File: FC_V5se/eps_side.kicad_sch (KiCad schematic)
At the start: 65 parts, among them IC6 LT3652IMSE#PBF, J10 INHIBIT_P2, J11 DF11CZ-12DP-2V(27), J14 Battery Input, J17 Face4 (Z- Face), J19 ISS_INHIBIT, J2 DF11CZ-12DP-2V(27), J20 RBF_Inhibit, J21 Heater Output, J23 Aux Deploy 1, J24 Deploy 2, J29 INHIBIT_S2, J7 INHIBIT_P1, J8 INHIBIT_S1, U10 TPS54226PWPRPWP14_2P31X2P46-L, U12 LT8610ABEMSE#TRPBF, U16 INA219AxDCN, U8 INA219AxDCN, U9 MCP23017_SS

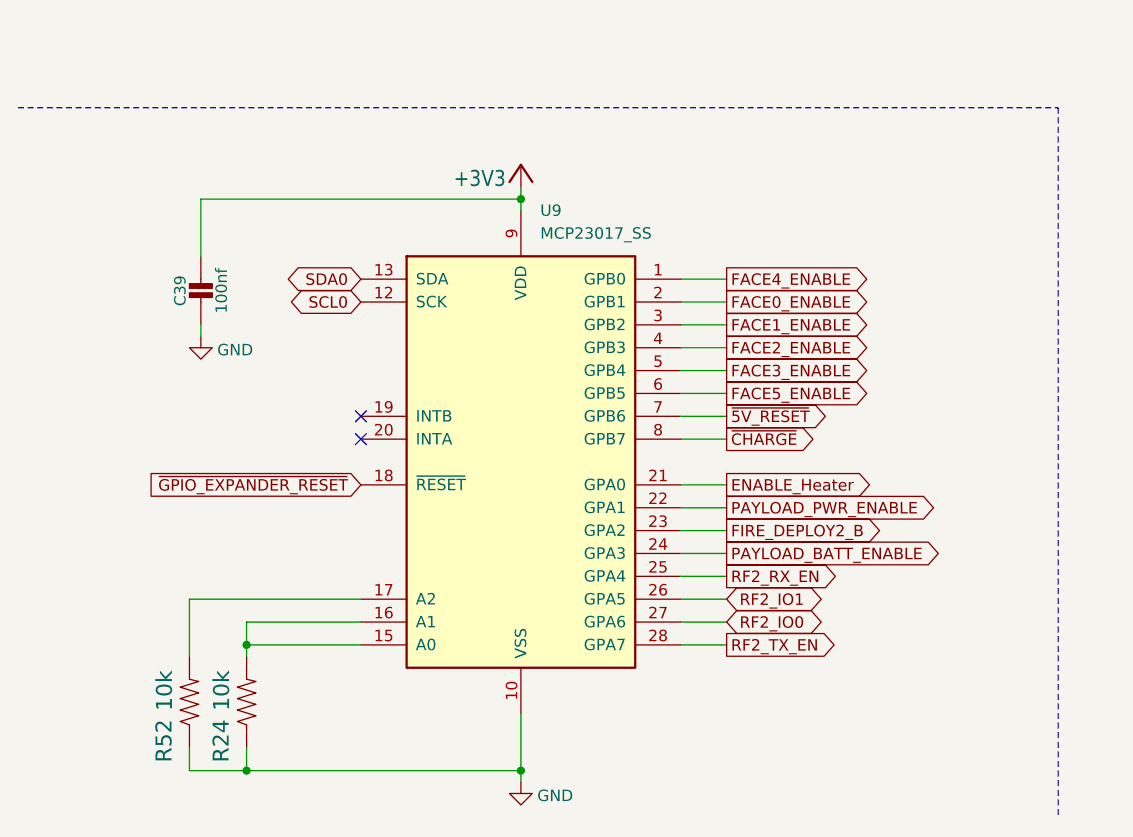
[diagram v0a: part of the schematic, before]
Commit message: V5e: Delete MCP23017
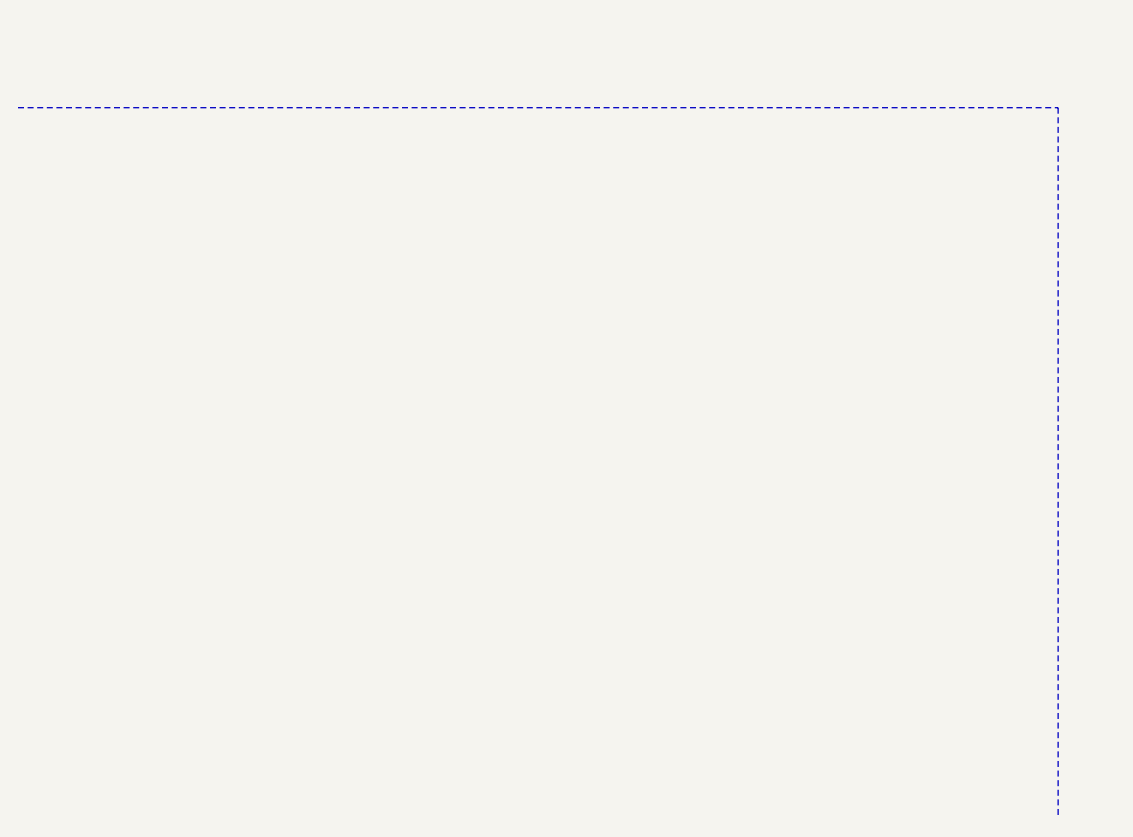
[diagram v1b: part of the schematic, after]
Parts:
- removed C39: 100nf, Capacitor_SMD:C_0402_1005Metric, symbol Adafruit ItsyBitsy RP2040-eagle-import:CAP_CERAMIC_0402NO
- removed R24, R52: 10k, Resistor_SMD:R_0603_1608Metric, symbol mainboard:RESISTOR0603
- removed U9: MCP23017_SS, Package_SO:SSOP-28_5.3x10.2mm_P0.65mm, symbol Interface_Expansion:MCP23017_SS
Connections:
- no-connect marks 8 -> 6
